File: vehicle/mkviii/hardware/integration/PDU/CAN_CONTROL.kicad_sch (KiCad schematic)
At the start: 11 parts, among them J10 CONN_02x03, J11 CONN_02x03, J5 CONN_02x03, J8 CONN_01X03, J9 CONN_02x03

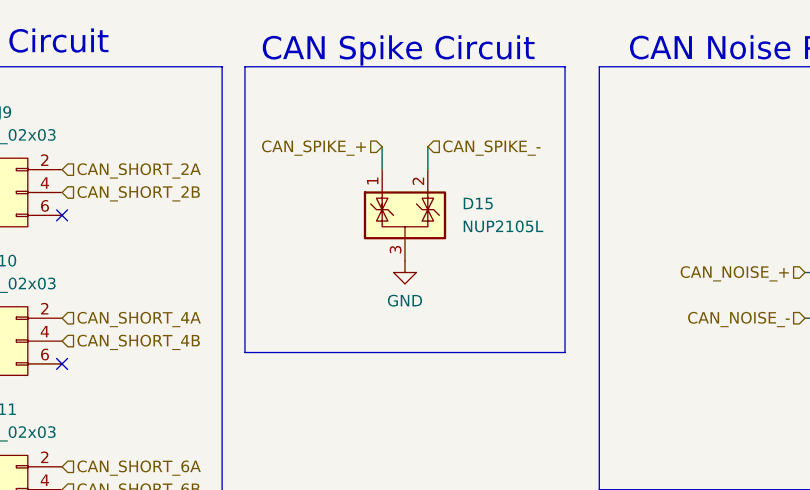
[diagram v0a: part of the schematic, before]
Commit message: Sort the parts together
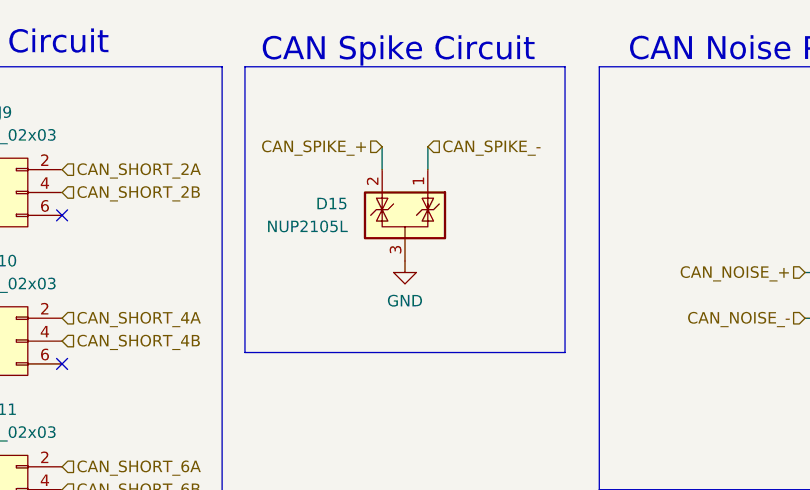
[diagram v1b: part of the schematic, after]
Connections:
- net CAN_SPIKE_+: now also D15.2 (K); no longer D15.1 (K)
- net CAN_SPIKE_-: now also D15.1 (K); no longer D15.2 (K)
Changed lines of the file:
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@@
 		(dnp no)
 		(fields_autoplaced yes)
-		(property "Reference" "#PWR042"
+		(property "Reference" "#PWR?"
 			(at 95.25 86.36 0)
 			(hide yes)
@@
 			(project "PDU"
 				(path "/f655fa78-2860-41ca-ba0e-06d986d434be/fb6a863c-99fa-4808-971d-be1b07470863"
-					(reference "#PWR042")
+					(reference "#PWR?")
 					(unit 1)
 				)
@@
 		(lib_id "Power_Protection:NUP2105L")
 		(at 95.25 74.93 0)
+		(mirror y)
 		(unit 1)
 		(body_style 1)
@@
 		(in_pos_files yes)
 		(dnp no)
-		(fields_autoplaced yes)
 		(property "Reference" "D15"
-			(at 101.6 73.6599 0)
+			(at 88.9 73.6599 0)
 			(show_name no)
 			(do_not_autoplace no)
@@
 		)
 		(property "Value" "NUP2105L"
-			(at 101.6 76.1999 0)
+			(at 88.9 76.1999 0)
 			(show_name no)
 			(do_not_autoplace no)
@@
 		)
 		(property "Footprint" "Package_TO_SOT_SMD:SOT-23"
-			(at 100.965 76.2 0)
+			(at 89.535 76.2 0)
 			(hide yes)
 			(show_name no)
@@
 		)
 		(property "Datasheet" "https://www.onsemi.com/pub_link/Collateral/NUP2105L-D.PDF"
-			(at 98.425 71.755 0)
-			(hide yes)
-			(show_name no)
+			(at 92.075 71.755 0)
+			(hide yes)
+			(show_name no)
